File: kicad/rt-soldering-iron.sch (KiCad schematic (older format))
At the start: 0 parts

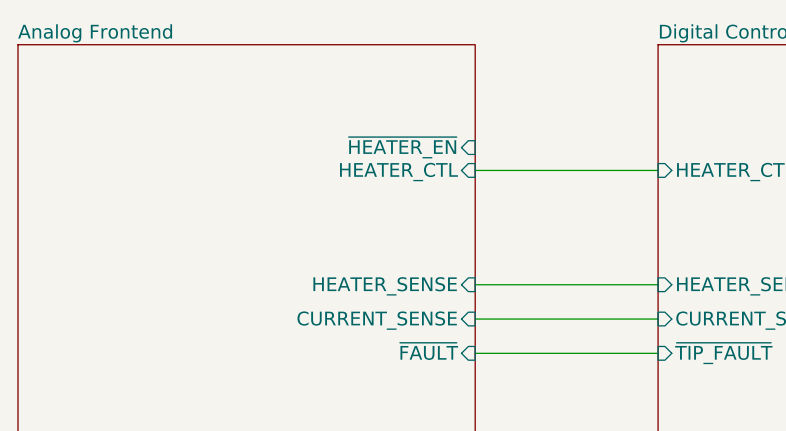
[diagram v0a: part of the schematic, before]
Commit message: Removed comp, efuse. Added zener protection. Fixed OLED footprint.
I may have destroyed a board by shorting the FB pin to ground. I left
off the zener protection on Rev A. Never again.
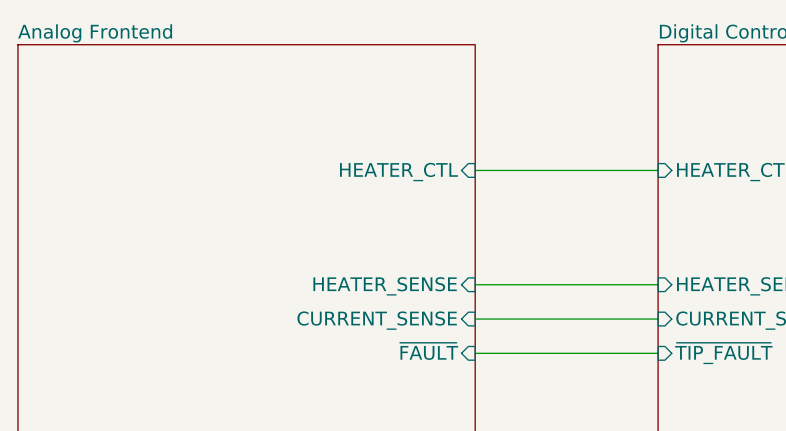
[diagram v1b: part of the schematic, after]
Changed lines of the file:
@@
 F4 "CURRENT_SENSE" I R 4600 3000 60
 F5 "~FAULT" I R 4600 3150 60
-F6 "~HEATER_EN" I R 4600 2250 60
 $EndSheet
 $Sheet

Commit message: Started second revision, added a comparator and eFuse
The comparator has no hysteresis in its current configuration, so that
will need to be fixed.
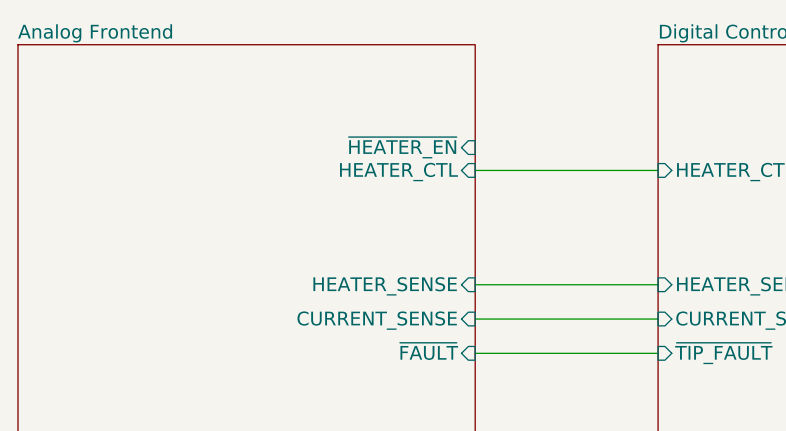
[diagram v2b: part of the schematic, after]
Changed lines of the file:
@@
 F4 "CURRENT_SENSE" I R 4600 3000 60
 F5 "~FAULT" I R 4600 3150 60
+F6 "~HEATER_EN" I R 4600 2250 60
 $EndSheet
 $Sheet
